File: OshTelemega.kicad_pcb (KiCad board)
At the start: 4 copper layers, 30 x 80 mm, 158 parts, among them J1 TAGCONNECT, J10 SERVOS, J2 Conn_01x02, J3 SMA_Edgelaunch, J4 USB_C_Receptacle_USB2.0_16P, J5 UFL, J6 RIGHT, J7 LEFT, J8 BATT, J9 Conn_02x05_Counter_Clockwise, Q1 SiA449DJ, Q2 AO3400A, Q3 SiA449DJ, Q4 SiA449DJ, U1 STM32L151VCTx, U10 MMC5983MA, U12 LM293QT, U13 LM293QT, U15 LM293QT, U17 MCP73831-2-OT, U18 TC2185-3.3VxCTTR, U19 W25Q64JVXGIQ, U2 WE-TVS-82400102, U20 SISB46DN, U21 SN74LVC1G80QDCKTQ1, U22 SISB46DN, U23 SISB46DN, U3 ADXL375, U4 MS5607-02BA, U5 MAX-M10S, U6 MCP130-xxxxTT, U7 DRV5012AEDMRR, U8 CC1200, U9 BMI088, X2 ECS-160-8-36Q-AES-TR1, Y1 ABM8W-40.0000MHZ

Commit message: changes to vias and silkscreens
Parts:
- moved J3 0.40 mm to (35.0, 22.5)
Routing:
- net GND: track 123.4 -> 123.6 mm, vias 236 -> 262
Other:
- board text added: "433MHz HAM"
- board text removed: "433MHZ HAM"

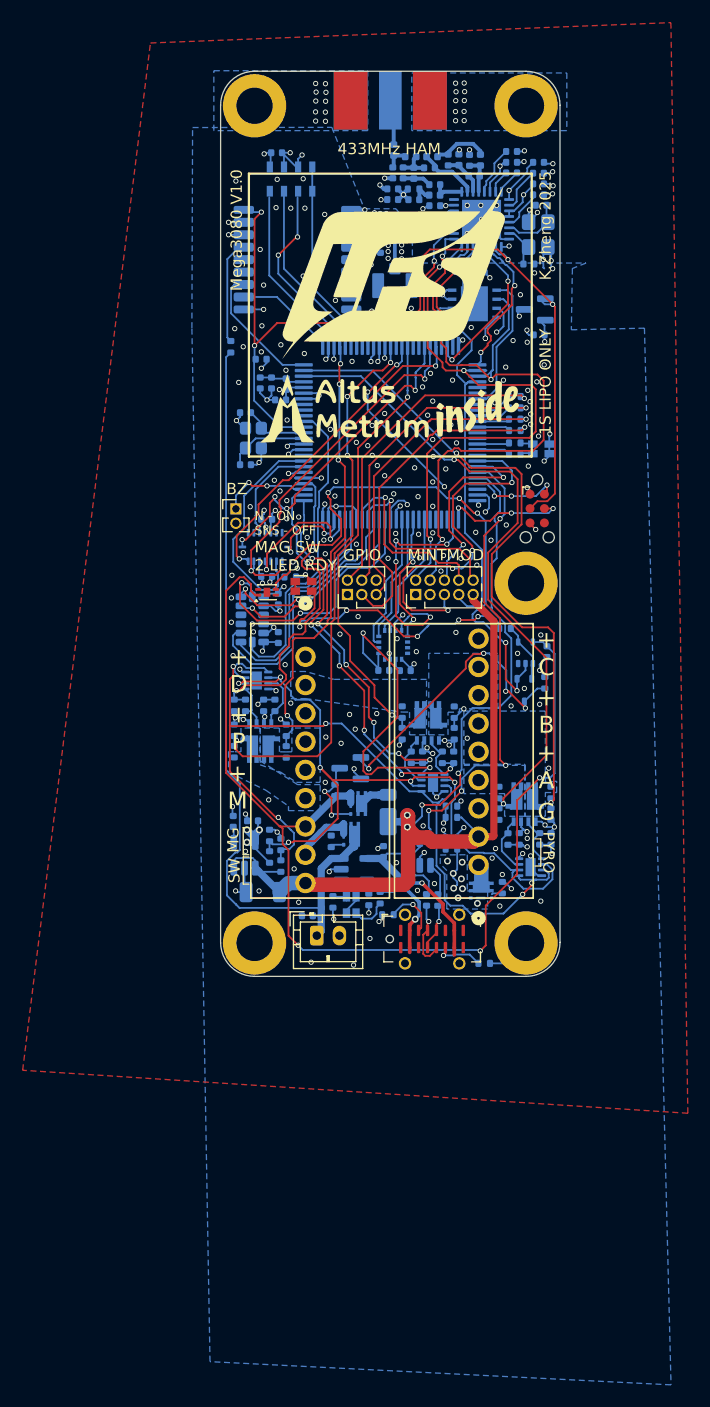
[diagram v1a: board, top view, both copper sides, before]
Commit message: resolved drc, added buzzer, and PPS led
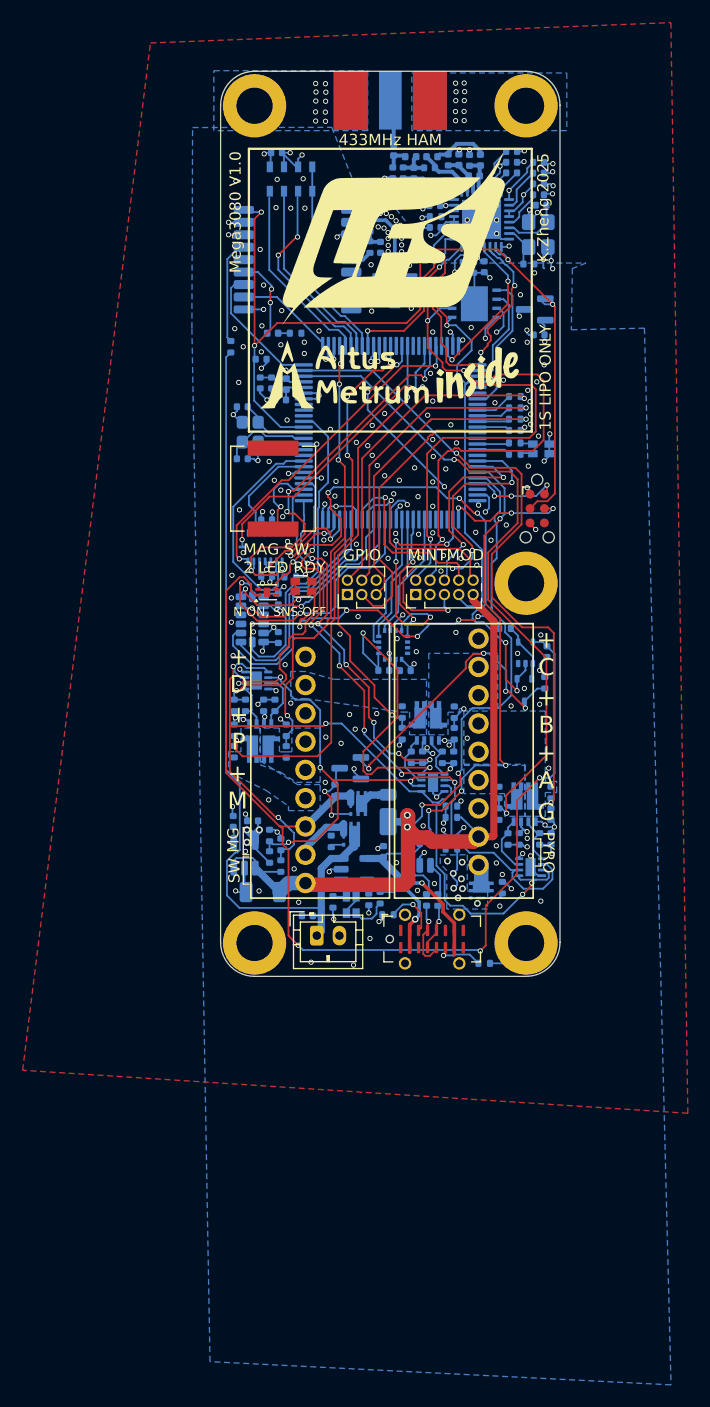
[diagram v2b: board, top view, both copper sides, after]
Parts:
- removed J2: Conn_01x02, Connector_PinHeader_1.27mm:PinHeader_1x02_P1.27mm_Vertical
- added D6: PPS, LED_SMD:LED_0402_1005Metric, B.Cu at (24.6, 43.1)
- added R56: 1k, Resistor_SMD:R_0402_1005Metric, B.Cu at (26.6, 43.1)
- added U11: CPE-171, FCU2025Lib:XDCR_CPT-7502-65-SMT-TR, F.Cu at (24.6, 56.8)
- moved G*** 3.00 mm to (35.0, 35.0)
- moved G*** 3.00 mm to (35.0, 46.8)
- moved C5 0.59 mm to (21.9, 49.6)
- moved C6 0.59 mm to (21.9, 54.2)
- moved X2 0.59 mm to (22.6, 51.9)
- moved C16 0.05 mm to (24.1, 59.6)
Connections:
- U5 pad 4: unconnected-(U5-TIMEPULSE-Pad4) -> Net-(D6-A)
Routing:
- net Net-(D6-A): track 0.00 -> 7.31 mm, vias 0 -> 2
- net /MISO1: track 32.8 -> 35.9 mm, vias 3 -> 5
- net /IMU_GYRO_INT: track 12.3 -> 10.8 mm
- net /SCK1: track 28.3 -> 26.9 mm, vias 4 -> 2
- net /SENSE_A: track 57.4 -> 58.8 mm
- net /CMP_RAIL: track 63.7 -> 62.4 mm
- net /IMU_ACCEL_INT: track 7.52 -> 6.50 mm
- net /PH1: track 5.20 -> 6.21 mm
- net Net-(D6-K): track 0.00 -> 0.90 mm
- net +3V3: track 89.7 -> 89.1 mm, vias 35 -> 34
- net GND: track 123.6 -> 123.0 mm, vias 262 -> 263
- net /NRST: track 81.8 -> 81.3 mm
- net /PH0: track 7.15 -> 7.71 mm
- net /BUZZ: track 7.55 -> 7.24 mm, vias 2 -> 1
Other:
- board text added: "N ON, SNS OFF"
- board text added: "PPS"
- board text removed: "+ G"
- board text removed: "BZ"
- board text removed: "N - ON SNS - OFF"

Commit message: silkscreen memes
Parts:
- added G***: LOGO, LOGO, F.Cu at (21.4, 50.3)
- added G***: LOGO, LOGO, B.Cu at (48.2, 47.6)
- added G***: LOGO, LOGO, B.Cu at (47.6, 79.5)
- moved U7 0.21 mm to (24.1, 65.8)
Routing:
- net +3V3: track 89.1 -> 88.4 mm
- net GND: vias 263 -> 264
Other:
- board text added: "CAUTION: Do Not Eat"
- board text added: "FLAMEY END DOWN"
- board text added: "Kev1n8088"
- board text added: "L1 GPS"
- board text added: "Leviathan Flight Systems"
- board text added: "N ON SNS OFF"
- board text added: "POINTY END UP"
- board text added: "SN:"
- board text added: "Warranty Void if Viewed"
- board text removed: "L1/L5 GPS"
- board text removed: "N ON, SNS OFF"

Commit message: tunes for production run 1
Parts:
- added G***: LOGO, LOGO, F.Cu at (44.8, 41.9)
- added G***: LOGO, LOGO, B.Cu at (39.4, 72.6)
- added G***: LOGO, LOGO, B.Cu at (44.5, 58.5)
- moved G*** 2.00 mm to (35.0, 37.0)
- moved G*** 1.20 mm to (35.0, 48.0)
- moved R35 0.30 mm to (21.2, 80.4)
- moved R14 0.29 mm to (49.2, 83.4)
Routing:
- net GND: track 123.0 -> 124.7 mm, vias 264 -> 278
- net Net-(J6-Pin_1): track 1.72 -> 0.00 mm
- added copper zone on B.Cu, net Net-(J6-Pin_1)
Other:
- board text added: "Leviathan Flight Systems Mega3080 V1.0 1S LIPO ONLY"
- board text removed: "1S LIPO ONLY"
- board text removed: "Leviathan Flight Systems"
- board text removed: "Mega3080 V1.0"
- board text removed: "SN:"
